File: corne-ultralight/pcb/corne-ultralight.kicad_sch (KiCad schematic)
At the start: 102 parts, among them J2 OLED, J7 OLED, SW1 SW_PUSH, SW10 SW_PUSH, SW11 SW_PUSH, SW12 SW_PUSH, SW13 SW_PUSH, SW14 SW_PUSH, SW15 SW_PUSH, SW16 SW_PUSH, SW17 SW_PUSH, SW18 SW_PUSH, SW19 SW_PUSH, SW2 SW_PUSH, SW20 SW_PUSH, SW21 SW_PUSH, SW22 SW_PUSH, SW23 SW_PUSH, SW24 SW_PUSH, SW25 SW_PUSH, SW26 SW_PUSH, SW27 SW_PUSH, SW28 SW_PUSH, SW29 SW_PUSH, SW3 SW_PUSH, SW30 SW_PUSH, SW31 SW_PUSH, SW32 SW_PUSH, SW33 SW_PUSH, SW34 SW_PUSH, SW35 SW_PUSH, SW36 SW_PUSH, SW37 SW_PUSH, SW38 SW_PUSH, SW39 SW_PUSH, SW4 SW_PUSH, SW40 SW_PUSH, SW41 SW_PUSH, SW42 SW_PUSH, SW5 SW_PUSH, SW6 SW_PUSH, SW7 SW_PUSH, SW8 SW_PUSH, SW9 SW_PUSH, U1 ProMicro, U2 ProMicro

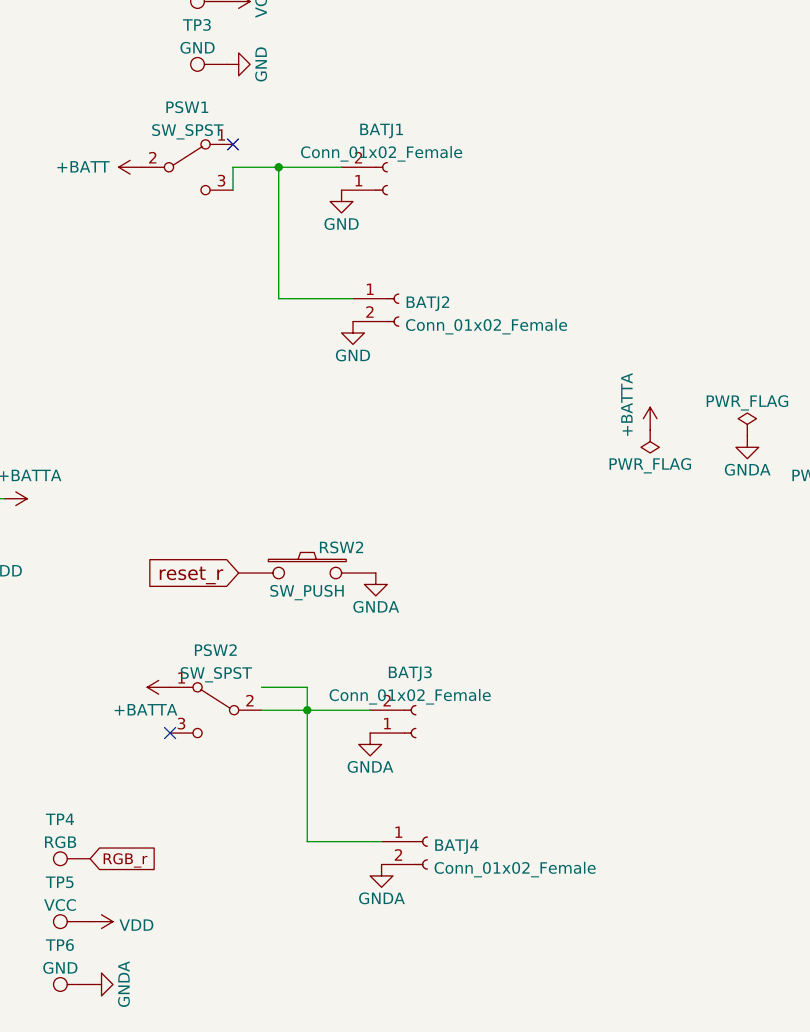
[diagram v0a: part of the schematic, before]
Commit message: Choc v1 hotswap
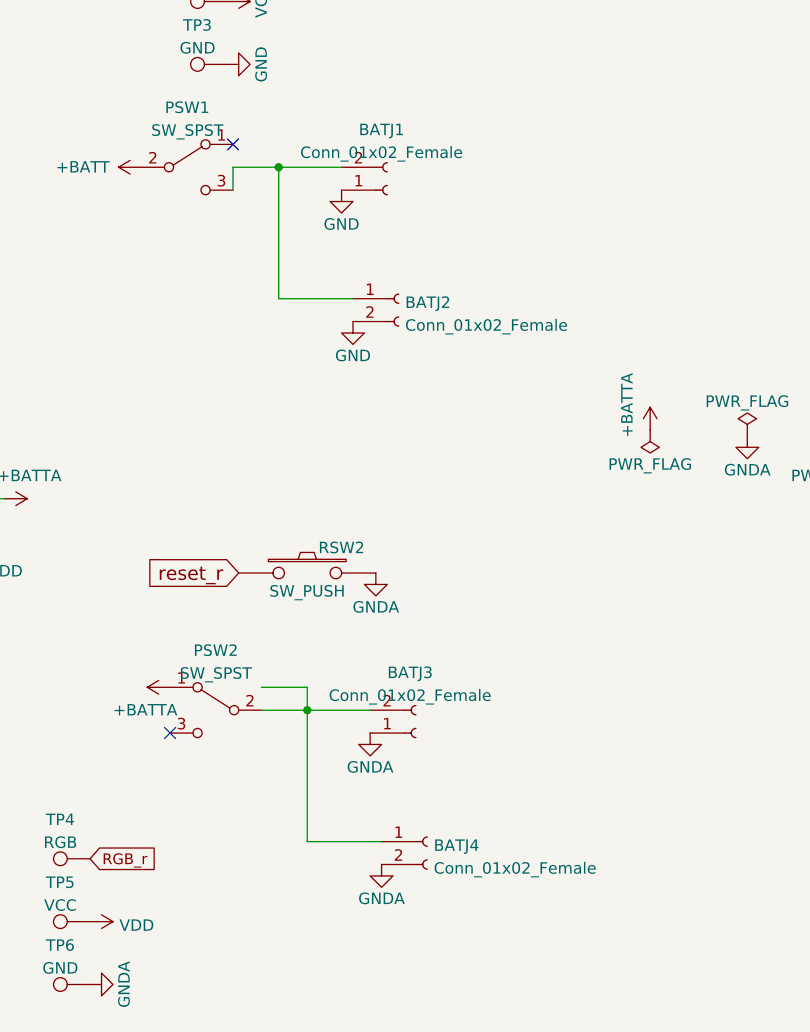
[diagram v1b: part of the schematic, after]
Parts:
- SW1, SW10, SW11, SW12, SW13, SW14, SW15, SW16, SW17, SW18, SW19, SW2, SW20, SW22, SW23, SW24, SW25, SW26, SW27, SW28, SW29, SW3, SW30, SW31, SW32, SW33, SW34, SW35, SW36, SW37, SW38, SW39, SW4, SW40, SW41, SW5, SW6, SW7, SW8, SW9: footprint gateron-ks27:gateron-ks27-choc-v1 -> ScottoKeebs_Hotswap:Hotswap_Choc_V1_Flipped
- SW21, SW42: footprint gateron-ks27:gateron-ks27-choc-v1-1.5u -> ScottoKeebs_Hotswap:Hotswap_Choc_V1_1.50u

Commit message: Switch to SMD only diodes, Finish routing
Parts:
- D1, D10, D11, D12, D13, D14, D15, D16, D17, D18, D19, D2, D20, D21, D22, D23, D24, D25, D26, D27, D28, D29, D3, D30, D31, D32, D33, D34, D35, D36, D37, D38, D39, D4, D40, D41, D42, D5, D6, D7, D8, D9: footprint kbd:D3_TH -> ScottoKeebs_Components:Diode_SOD-123
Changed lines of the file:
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@@
 			)
 		)
-		(property "Footprint" "kbd:D3_TH"
+		(property "Footprint" "ScottoKeebs_Components:Diode_SOD-123"
 			(at 48.895 27.94 0)
 			(effects
@@
 			)
 		)
-		(property "Footprint" "kbd:D3_TH"
+		(property "Footprint" "ScottoKeebs_Components:Diode_SOD-123"
 			(at 66.675 27.94 0)
 			(effects
@@
 			)
 		)
-		(property "Footprint" "kbd:D3_TH"
+		(property "Footprint" "ScottoKeebs_Components:Diode_SOD-123"
 			(at 84.455 27.94 0)
 			(effects
@@
 			)
 		)
-		(property "Footprint" "kbd:D3_TH"
+		(property "Footprint" "ScottoKeebs_Components:Diode_SOD-123"
 			(at 102.235 27.94 0)
 			(effects
@@
 			)
 		)
-		(property "Footprint" "kbd:D3_TH"
+		(property "Footprint" "ScottoKeebs_Components:Diode_SOD-123"
 			(at 120.015 27.94 0)
 			(effects
@@
 			)
 		)
-		(property "Footprint" "kbd:D3_TH"
+		(property "Footprint" "ScottoKeebs_Components:Diode_SOD-123"
 			(at 31.115 27.94 0)
 			(effects
@@
 			)
 		)
-		(property "Footprint" "kbd:D3_TH"
+		(property "Footprint" "ScottoKeebs_Components:Diode_SOD-123"
 			(at 48.895 43.18 0)
 			(effects
@@
 			)
 		)
-		(property "Footprint" "kbd:D3_TH"
+		(property "Footprint" "ScottoKeebs_Components:Diode_SOD-123"
 			(at 66.675 43.18 0)
 			(effects
@@
 			)
 		)
-		(property "Footprint" "kbd:D3_TH"
+		(property "Footprint" "ScottoKeebs_Components:Diode_SOD-123"
 			(at 84.455 43.18 0)
 			(effects
@@
 			)
 		)
-		(property "Footprint" "kbd:D3_TH"
+		(property "Footprint" "ScottoKeebs_Components:Diode_SOD-123"
 			(at 102.235 43.18 0)
 			(effects
@@
 			)
 		)
-		(property "Footprint" "kbd:D3_TH"
+		(property "Footprint" "ScottoKeebs_Components:Diode_SOD-123"
 			(at 120.015 43.18 0)
 			(effects
@@
 			)
 		)
-		(property "Footprint" "kbd:D3_TH"
+		(property "Footprint" "ScottoKeebs_Components:Diode_SOD-123"
 			(at 31.115 43.18 0)
 			(effects
@@
 			)
 		)
-		(property "Footprint" "kbd:D3_TH"
+		(property "Footprint" "ScottoKeebs_Components:Diode_SOD-123"
 			(at 48.895 58.42 0)
 			(effects
@@
 			)
 		)
-		(property "Footprint" "kbd:D3_TH"
+		(property "Footprint" "ScottoKeebs_Components:Diode_SOD-123"
 			(at 66.675 58.42 0)
 			(effects
@@
 			)
 		)
-		(property "Footprint" "kbd:D3_TH"
+		(property "Footprint" "ScottoKeebs_Components:Diode_SOD-123"
 			(at 84.455 58.42 0)
 			(effects
@@
 			)
 		)
-		(property "Footprint" "kbd:D3_TH"
+		(property "Footprint" "ScottoKeebs_Components:Diode_SOD-123"
 			(at 102.235 58.42 0)
 			(effects
@@
 			)
 		)
-		(property "Footprint" "kbd:D3_TH"
+		(property "Footprint" "ScottoKeebs_Components:Diode_SOD-123"
 			(at 120.015 58.42 0)
 			(effects
@@
 			)
 		)
-		(property "Footprint" "kbd:D3_TH"
+		(property "Footprint" "ScottoKeebs_Components:Diode_SOD-123"
 			(at 31.115 58.42 0)
 			(effects
@@
 			)
 		)
-		(property "Footprint" "kbd:D3_TH"
+		(property "Footprint" "ScottoKeebs_Components:Diode_SOD-123"
 			(at 102.235 73.66 0)
 			(effects
@@
 			)
 		)
-		(property "Footprint" "kbd:D3_TH"
+		(property "Footprint" "ScottoKeebs_Components:Diode_SOD-123"
 			(at 120.015 73.66 0)
 			(effects
@@
 			)
 		)
-		(property "Footprint" "kbd:D3_TH"
+		(property "Footprint" "ScottoKeebs_Components:Diode_SOD-123"
 			(at 84.455 73.66 0)
 			(effects
@@
 			)
 		)
-		(property "Footprint" "kbd:D3_TH"
+		(property "Footprint" "ScottoKeebs_Components:Diode_SOD-123"
 			(at 49.53 110.49 0)
 			(effects
@@
 			)
 		)
-		(property "Footprint" "kbd:D3_TH"
+		(property "Footprint" "ScottoKeebs_Components:Diode_SOD-123"
 			(at 67.31 110.49 0)
 			(effects
@@
 			)
 		)
-		(property "Footprint" "kbd:D3_TH"
+		(property "Footprint" "ScottoKeebs_Components:Diode_SOD-123"
 			(at 85.09 110.49 0)
 			(effects
@@
 			)
 		)
-		(property "Footprint" "kbd:D3_TH"
+		(property "Footprint" "ScottoKeebs_Components:Diode_SOD-123"
 			(at 102.87 110.49 0)
 			(effects
@@
 			)
 		)
-		(property "Footprint" "kbd:D3_TH"
+		(property "Footprint" "ScottoKeebs_Components:Diode_SOD-123"
 			(at 120.65 110.49 0)
 			(effects
@@
 			)
 		)
-		(property "Footprint" "kbd:D3_TH"
+		(property "Footprint" "ScottoKeebs_Components:Diode_SOD-123"
 			(at 31.75 110.49 0)
 			(effects
@@
 			)
 		)
-		(property "Footprint" "kbd:D3_TH"
+		(property "Footprint" "ScottoKeebs_Components:Diode_SOD-123"
 			(at 49.53 125.73 0)
 			(effects
@@
 			)
 		)
-		(property "Footprint" "kbd:D3_TH"
+		(property "Footprint" "ScottoKeebs_Components:Diode_SOD-123"
 			(at 67.31 125.73 0)
 			(effects
@@
 			)
 		)
-		(property "Footprint" "kbd:D3_TH"
+		(property "Footprint" "ScottoKeebs_Components:Diode_SOD-123"
 			(at 85.09 125.73 0)
 			(effects
@@
 			)
 		)
-		(property "Footprint" "kbd:D3_TH"
+		(property "Footprint" "ScottoKeebs_Components:Diode_SOD-123"
 			(at 102.87 125.73 0)
 			(effects
@@
 			)
 		)
-		(property "Footprint" "kbd:D3_TH"
+		(property "Footprint" "ScottoKeebs_Components:Diode_SOD-123"
 			(at 120.65 125.73 0)
 			(effects
@@
 			)
 		)
-		(property "Footprint" "kbd:D3_TH"
+		(property "Footprint" "ScottoKeebs_Components:Diode_SOD-123"
 			(at 31.75 125.73 0)
 			(effects
@@
 			)
 		)
-		(property "Footprint" "kbd:D3_TH"
+		(property "Footprint" "ScottoKeebs_Components:Diode_SOD-123"
 			(at 49.53 140.97 0)
 			(effects
@@
 			)
 		)
-		(property "Footprint" "kbd:D3_TH"
+		(property "Footprint" "ScottoKeebs_Components:Diode_SOD-123"
 			(at 67.31 140.97 0)
 			(effects
@@
 			)
 		)
-		(property "Footprint" "kbd:D3_TH"
+		(property "Footprint" "ScottoKeebs_Components:Diode_SOD-123"
 			(at 85.09 140.97 0)
 			(effects
@@
 			)
 		)
-		(property "Footprint" "kbd:D3_TH"
+		(property "Footprint" "ScottoKeebs_Components:Diode_SOD-123"
 			(at 102.87 140.97 0)
 			(effects
@@
 			)
 		)
-		(property "Footprint" "kbd:D3_TH"
+		(property "Footprint" "ScottoKeebs_Components:Diode_SOD-123"
 			(at 120.65 140.97 0)
 			(effects
@@
 			)
 		)
-		(property "Footprint" "kbd:D3_TH"
+		(property "Footprint" "ScottoKeebs_Components:Diode_SOD-123"
 			(at 31.75 140.97 0)
 			(effects
@@
 			)
 		)
-		(property "Footprint" "kbd:D3_TH"
+		(property "Footprint" "ScottoKeebs_Components:Diode_SOD-123"
 			(at 102.87 156.21 0)
 			(effects
@@
 			)
 		)
-		(property "Footprint" "kbd:D3_TH"
+		(property "Footprint" "ScottoKeebs_Components:Diode_SOD-123"
 			(at 120.65 156.21 0)
 			(effects
@@
 			)
 		)
-		(property "Footprint" "kbd:D3_TH"
+		(property "Footprint" "ScottoKeebs_Components:Diode_SOD-123"
 			(at 85.09 156.21 0)
 			(effects
